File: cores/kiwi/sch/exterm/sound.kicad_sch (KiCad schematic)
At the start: 38 parts, among them J16 HA1388

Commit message: Schematics PDF moved to JTBIN
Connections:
- net ~{RST} renamed ~{MCU_RST}
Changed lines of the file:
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@@
     (effects (font (size 1.27 1.27)) (justify left))
   )
-  (hierarchical_label "~{RST}" (shape output) (at 355.6 62.23 0)
+  (hierarchical_label "~{MCU_RST}" (shape output) (at 355.6 62.23 0)
     (effects (font (size 1.27 1.27)) (justify left))
   )

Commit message: issue#46
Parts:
- added B3, B7: 74LS74, symbol jt74:74LS74
- added C4, C5: 74LS245, symbol jt74:74LS245
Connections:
- net MAIN_~{RD}: now also C5.1 (A->B)
- net SHD0: now also C4.11 (B7), C5.11 (B7)
- net SHD1: now also C4.12 (B6), C5.12 (B6)
- net SHD2: now also C4.13 (B5), C5.13 (B5)
- net SHD3: now also C4.14 (B4), C5.14 (B4)
- net SHD4: now also C4.15 (B3), C5.15 (B3)
- net SHD5: now also C4.16 (B2), C5.16 (B2)
- net SHD6: now also C4.17 (B1), C5.17 (B1)
- net SHD7: now also C4.18 (B0), C5.18 (B0)
- net SND_D0: now also C4.9 (A7)
- net SND_D1: now also C4.8 (A6)
- net SND_D2: now also C4.7 (A5)
- net SND_D3: now also C4.6 (A4)
- net SND_D4: now also C4.5 (A3)
- net SND_D5: now also C4.4 (A2)
- net SND_D6: now also C4.3 (A1)
- net SND_D7: now also C4.2 (A0)
- net SND_~{INT}: now also B7.8 (~{Q})
- net SND_~{RD}: now also C4.1 (A->B)
- net S_~{IORQ}: now also B7.13 (~{R})
- net VCC: now also B3.1 (~{R}), B3.10 (~{S}), B3.13 (~{R}), B7.10 (~{S}), B7.12 (D)
- net YM_~{CS}: now also B3.2 (D)
- net at SWB2.10, YM_F8.32 (IOB6): now also SWB2.9, YM_F8.33 (IOB7)
- net at SWB2.11, YM_F8.31 (IOB5): now also SWB2.12, YM_F8.30 (IOB4)
- net at SWB2.13, YM_F8.29 (IOB3): now also SWB2.14, YM_F8.28 (IOB2)
- net at SWB2.15, YM_F8.27 (IOB1): now also SWB2.16, YM_F8.26 (IOB0)
- net CLK_SND renamed H0_BUF
- net H0_BUF: now also B3.11 (C), B3.3 (C), B7.11 (C)
- net PHM renamed H2_BUF
- new net: B3.12 (D), B3.5 (Q)
- new net MAIN_VD10: C5.7 (A5)
- new net MAIN_VD11: C5.6 (A4)
- new net MAIN_VD12: C5.5 (A3)
- new net MAIN_VD13: C5.4 (A2)
- new net MAIN_VD14: C5.3 (A1)
- new net MAIN_VD15: C5.2 (A0)
- new net MAIN_VD8: C5.9 (A7)
- new net MAIN_VD9: C5.8 (A6)
- new net SND_CLK': B3.4 (~{S}), B3.9 (Q)
- new net ~{SBNKMWR}: C5.19 (~{CE})
- new net ~{SBNKSWR}: C4.19 (~{CE})
- new net ~{SND_CLK'}: B3.6 (~{Q})
- no-connect marks 14 -> 16
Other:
- moved on the sheet: C8, CC10, CC12, R21, R6, R9, RV1, SWA1, SWB2

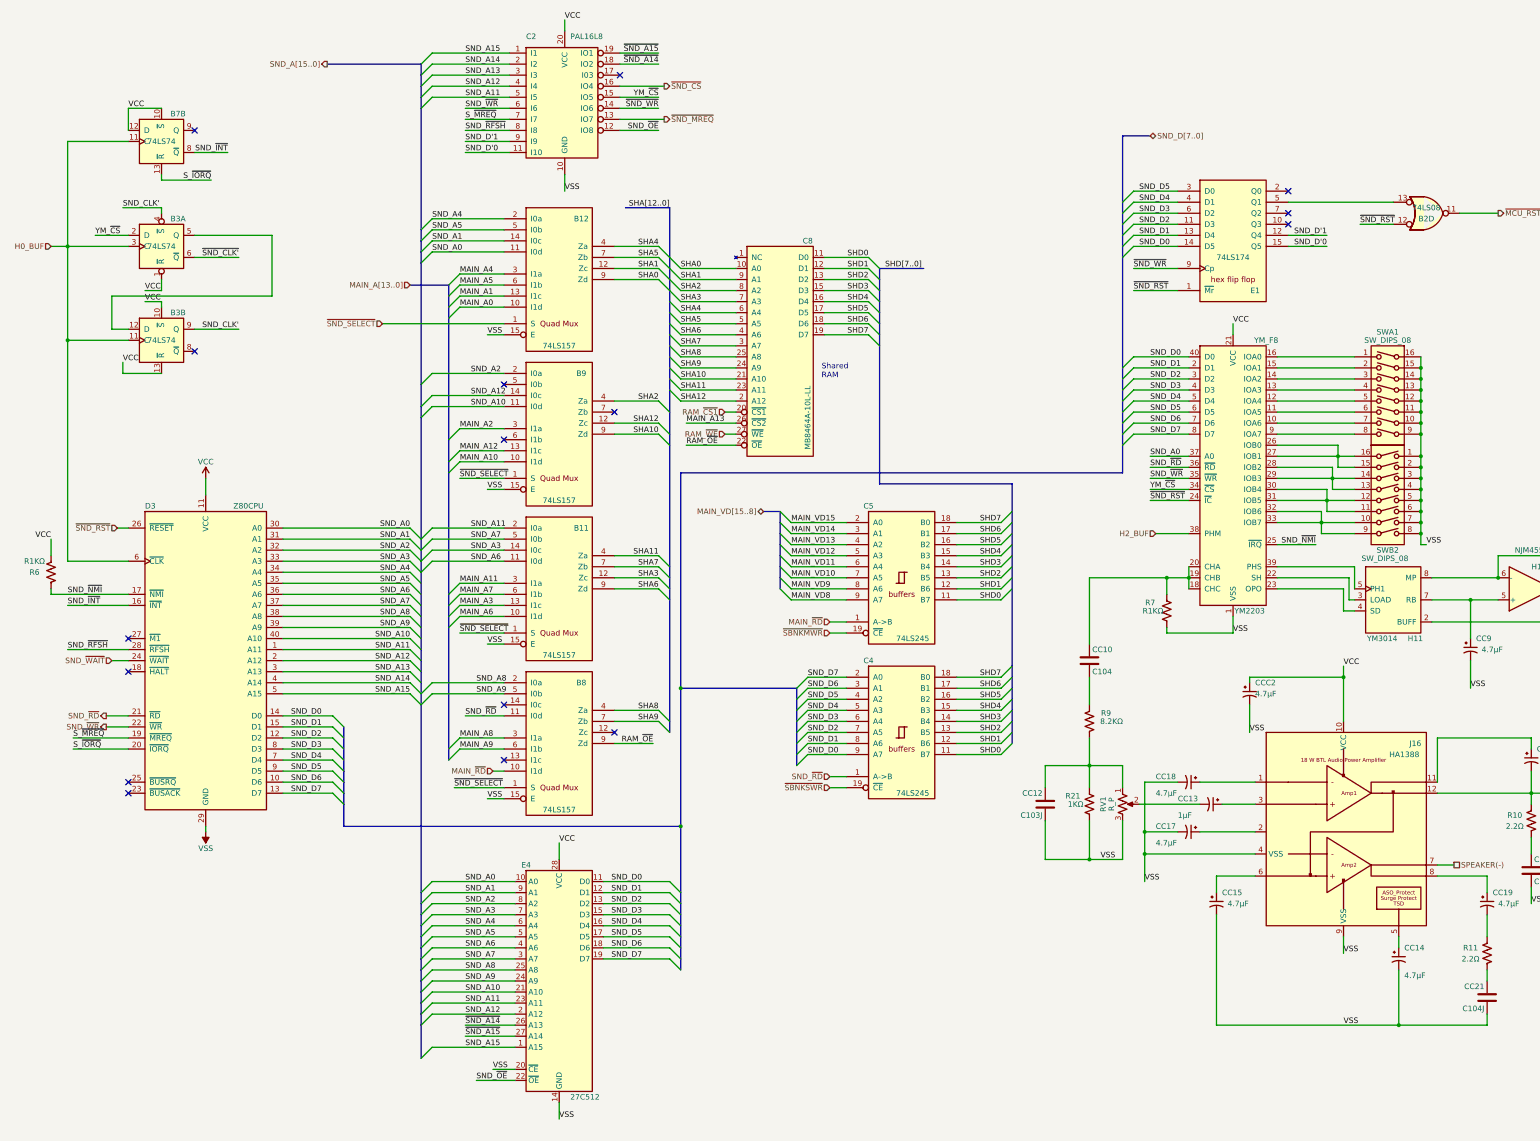
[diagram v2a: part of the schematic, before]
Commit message: sheet_size_update
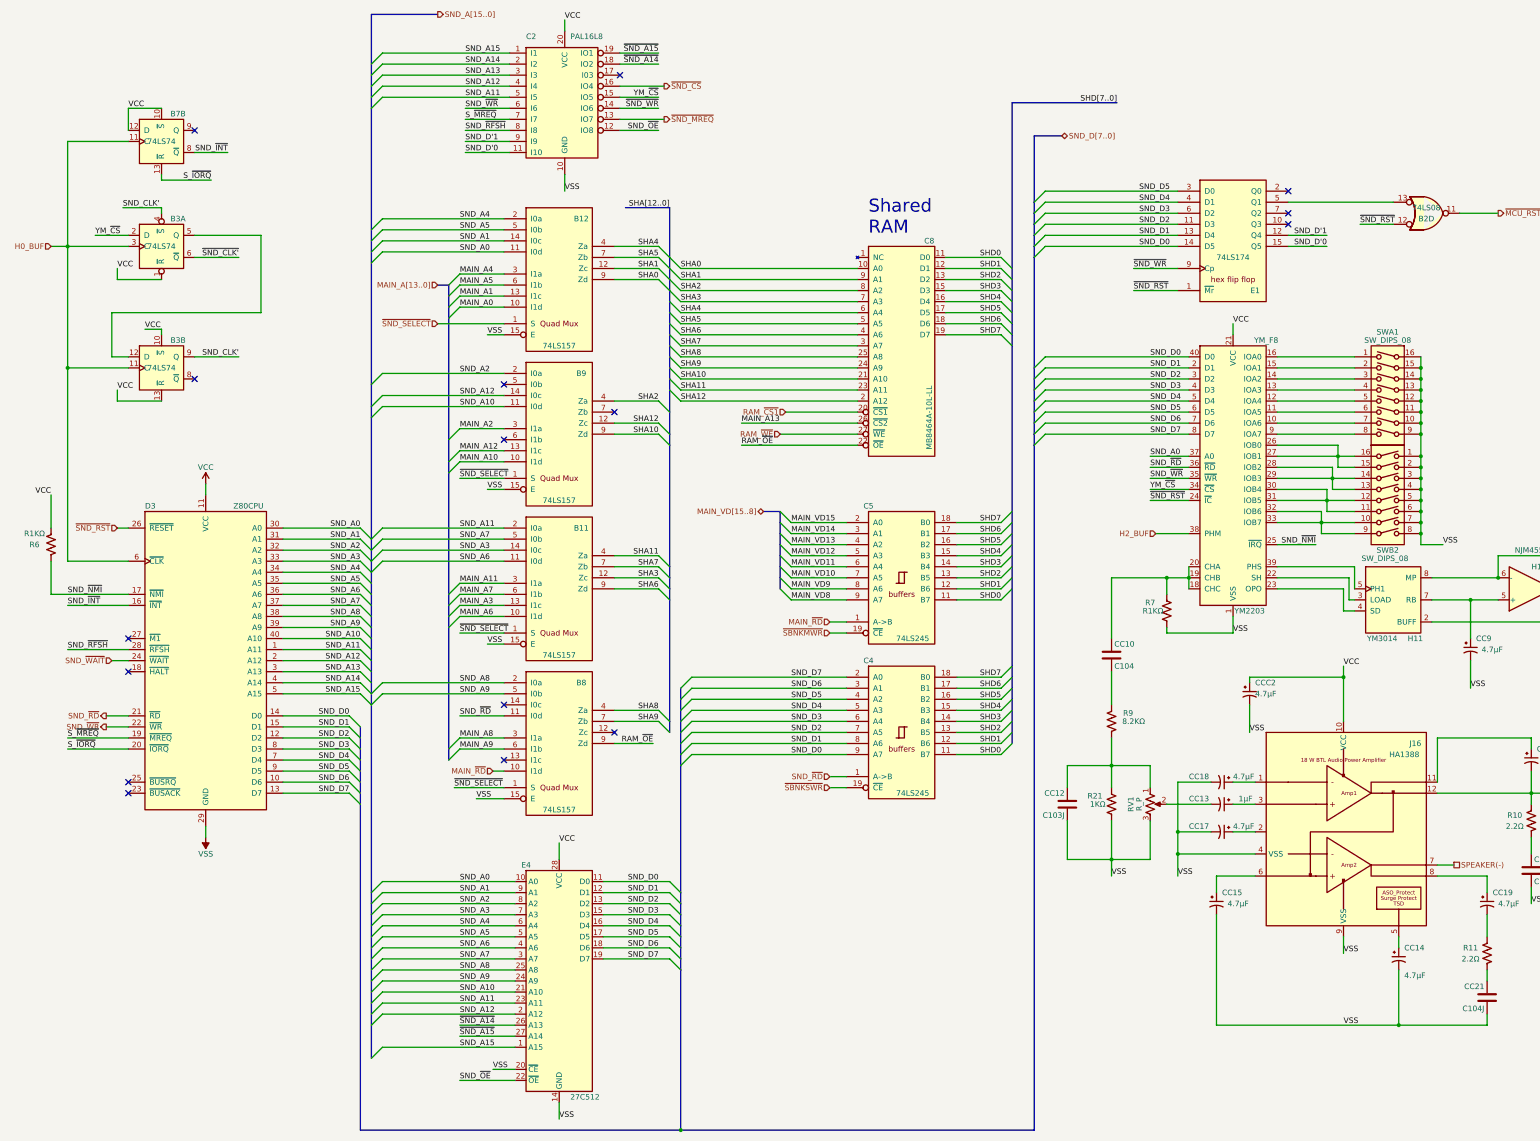
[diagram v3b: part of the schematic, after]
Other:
- moved on the sheet: B3B, C8, CC10, CC12, CC13, CC17, CC18, R21, R6, R9, RV1
